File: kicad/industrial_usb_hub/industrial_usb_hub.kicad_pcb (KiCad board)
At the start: 4 copper layers, 55.5 x 64 mm, 86 parts, among them J1 USB3_A, J2 USB_C_Receptacle, J3 USB3_A, J4 USB3_A, J6 USB3_A, U1 USB5744-I_2G, U2 HD3SS3212IRKSR, U3 TUSB321, U4 SY6280, U5 SY6280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

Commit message: routed the USB C cables, fuck that was annoying, but at some point it just, got easier randomly? at an instant, didn't even notice it
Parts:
- moved R24 12.2 mm to (127.1, 114.5)
- moved U3 11.3 mm to (128.5, 117.8)
- moved C24 9.29 mm to (141.9, 112.7)
- moved C23 3.01 mm to (142.0, 110.8)
- moved Y1 2.82 mm to (138.6, 111.2)
- moved C13 2.77 mm to (132.3, 112.2)
- moved U2 2.59 mm to (135.2, 117.1)
- moved C14 2.57 mm to (133.1, 112.2)
- moved R1 2.36 mm to (132.0, 119.8)
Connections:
- net Net-(U1-USB3UP_TXDM) renamed /Hub Controller/USB3UP_TXD_N
- net Net-(U1-USB3UP_TXDP) renamed /Hub Controller/USB3UP_TXD_P
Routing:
- net /Upstream/RX1_N: track 0.00 -> 27.5 mm
- net /Upstream/RX1_P: track 0.00 -> 24.5 mm, vias 0 -> 2
- net /Upstream/TX2_N: track 0.00 -> 16.2 mm
- net Net-(J2-CC2): track 0.00 -> 15.7 mm
- net /Hub Controller/UP_D_N: track 0.00 -> 15.7 mm
- net /Hub Controller/UP_D_P: track 0.00 -> 15.7 mm
- net /Upstream/TX2_P: track 0.00 -> 13.0 mm
- net Net-(J2-CC1): track 0.00 -> 10.5 mm, vias 0 -> 2
- net Net-(U1-XTALO): track 0.00 -> 9.72 mm
- net /Hub Controller/UP_RX_P: track 0.00 -> 8.75 mm, vias 0 -> 1
- net /Hub Controller/UP_RX_N: track 0.00 -> 8.73 mm, vias 0 -> 1
- net Net-(U1-XTALI/CLK_IN): track 0.00 -> 7.84 mm
- net /Upstream/RX2_P: track 0.00 -> 5.03 mm, vias 0 -> 1
- net /Upstream/RX2_N: track 0.00 -> 5.00 mm, vias 0 -> 1
- net /Hub Controller/UP_TX_P: track 0.00 -> 4.12 mm, vias 0 -> 1
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
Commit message: okay okay it seems easier to do differential routing, feels menacing tho
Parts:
- moved C24 6.54 mm to (135.5, 111.6)
- moved C23 6.48 mm to (135.6, 109.8)
- moved C33 0.94 mm to (126.1, 103.2), turned to -90 degrees
- moved C29 0.83 mm to (130.0, 99.5)
- moved C30 0.77 mm to (130.0, 100.2)
- moved R11 0.23 mm to (128.6, 107.0)
- moved R12 0.23 mm to (128.6, 107.8)
- moved R13 0.19 mm to (128.6, 106.3)
- moved R14 0.18 mm to (128.5, 105.6)
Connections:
- C29 pad 1: Net-(U1-USB3DN_TXDP4) -> /Hub Controller/DN_TX_P4
- C29 pad 2: /Downstream/DN_TX_P4 -> /Hub Controller/DN_TX_P4
- C30 pad 1: Net-(U1-USB3DN_TXDM4) -> /Hub Controller/DN_TX_N4
- C30 pad 2: /Downstream/DN_TX_N4 -> /Hub Controller/DN_TX_N4
- J3 pad 8: /Downstream/DN_TX_N4 -> /Hub Controller/DN_TX_N4
- J3 pad 9: /Downstream/DN_TX_P4 -> /Hub Controller/DN_TX_P4
- U1 pad 26: Net-(U1-USB3DN_TXDP4) -> /Hub Controller/DN_TX_P4
- U1 pad 27: Net-(U1-USB3DN_TXDM4) -> /Hub Controller/DN_TX_N4
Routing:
- net /Hub Controller/DN_TX_P4: track 0.00 -> 14.9 mm
- net /Hub Controller/DN_TX_N4: track 0.00 -> 14.0 mm
- net /Downstream/DN_RX_N4: track 0.00 -> 12.1 mm
- net /Downstream/DN_RX_P4: track 0.00 -> 11.4 mm
- net Net-(U2-SEL): track 2.84 -> 13.9 mm, vias 0 -> 1
- net Net-(U3-VBUS_DET): track 0.00 -> 3.82 mm
- net Net-(U1-XTALO): track 9.72 -> 6.03 mm
- net Net-(U1-~{RESET}): track 0.00 -> 3.53 mm
- net Net-(U1-VBUS_DET): track 0.00 -> 3.44 mm
- net Net-(U1-XTALI/CLK_IN): track 7.84 -> 5.85 mm
- net /Hub Controller/SPI_CE_N: track 0.00 -> 1.63 mm
- net /Hub Controller/SPI_DI: track 0.00 -> 1.44 mm
- net /Hub Controller/SPI_CLK: track 0.00 -> 1.39 mm
- net /Hub Controller/SPI_DO: track 0.00 -> 1.29 mm
- net /Downstream/DN_D_P4: track 0.00 -> 0.98 mm, vias 0 -> 1
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
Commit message: done routing, now fixing DRC errors (it's hatin)
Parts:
- C15, C16, C17, C18: moved to B.Cu
- moved C15 8.14 mm to (135.2, 114.0), turned to 180 degrees
- moved C16 7.83 mm to (135.3, 114.8), turned to 180 degrees
- moved C19 4.42 mm to (141.2, 106.3)
- moved C20 4.42 mm to (145.7, 107.6)
- moved R2 4.42 mm to (145.7, 105.8)
- moved U4 4.42 mm to (143.2, 106.3)
- moved C18 3.13 mm to (139.2, 106.0)
- moved C17 3.10 mm to (139.2, 106.7)
- moved C36 1.91 mm to (123.1, 86.7)
- moved R9 1.91 mm to (123.1, 88.2)
- moved U7 1.75 mm to (125.7, 87.2)
- moved R24 1.64 mm to (128.0, 116.0)
- moved C1 1.19 mm to (137.4, 97.5)
- moved C10 1.19 mm to (138.9, 97.5)
- moved C11 1.19 mm to (138.9, 96.8)
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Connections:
- net Net-(U1-USB3DN_TXDM1) renamed /Hub Controller/USB3_DN_TX_N1
- net Net-(U1-USB3DN_TXDM2) renamed /Hub Controller/USB3_DN_TX_N2
- net Net-(U1-USB3DN_TXDM3) renamed /Hub Controller/USB3_DN_TX_N3
- net Net-(U1-USB3DN_TXDP1) renamed /Hub Controller/USB3_DN_TX_P1
- net Net-(U1-USB3DN_TXDP2) renamed /Hub Controller/USB3_DN_TX_P2
- net Net-(U1-USB3DN_TXDP3) renamed /Hub Controller/USB3_DN_TX_P3
- C29 pad 1: /Hub Controller/DN_TX_P4 -> /Hub Controller/USB3_DN_TX_P4
- C29 pad 2: /Hub Controller/DN_TX_P4 -> /Downstream/DN_TX_P4
- C30 pad 1: /Hub Controller/DN_TX_N4 -> /Hub Controller/USB3_DN_TX_N4
- C30 pad 2: /Hub Controller/DN_TX_N4 -> /Downstream/DN_TX_N4
- J3 pad 8: /Hub Controller/DN_TX_N4 -> /Downstream/DN_TX_N4
- J3 pad 9: /Hub Controller/DN_TX_P4 -> /Downstream/DN_TX_P4
- U1 pad 26: /Hub Controller/DN_TX_P4 -> /Hub Controller/USB3_DN_TX_P4
- U1 pad 27: /Hub Controller/DN_TX_N4 -> /Hub Controller/USB3_DN_TX_N4
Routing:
- net GND: track 0.00 -> 71.5 mm, vias 0 -> 20
- net +1V2: track 0.00 -> 44.2 mm, vias 0 -> 7
- net /Downstream/DN_D_P3: track 0.00 -> 41.7 mm, vias 0 -> 1
- net /Downstream/DN_D_N3: track 0.00 -> 41.6 mm, vias 0 -> 1
- net /Downstream/DN_D_N2: track 0.00 -> 38.0 mm, vias 0 -> 1
- net /Downstream/DN_D_P2: track 0.00 -> 38.0 mm, vias 0 -> 1
- net /Downstream/EN2: track 0.00 -> 36.0 mm, vias 0 -> 2
- net /Downstream/DN_RX_N2: track 0.00 -> 35.6 mm, vias 0 -> 1
- net /Downstream/DN_RX_P2: track 0.00 -> 35.6 mm, vias 0 -> 1
- net +3V3: track 0.00 -> 35.0 mm, vias 0 -> 5
- net /Downstream/DN_TX_P3: track 0.00 -> 31.8 mm
- net /Downstream/DN_TX_N3: track 0.00 -> 31.7 mm
- net /Downstream/DN_RX_P3: track 0.00 -> 31.3 mm
- net /Downstream/DN_RX_N3: track 0.00 -> 31.3 mm
- net Net-(J4-VBUS): track 0.00 -> 30.7 mm
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- added copper zone on In2.Cu, net +1V2
- added copper zone on In2.Cu, net +3V3
- added copper zone on In2.Cu, net /Downstream/VBUS
- added copper zone on B.Cu, net GND
- added copper zone on F.Cu, net GND

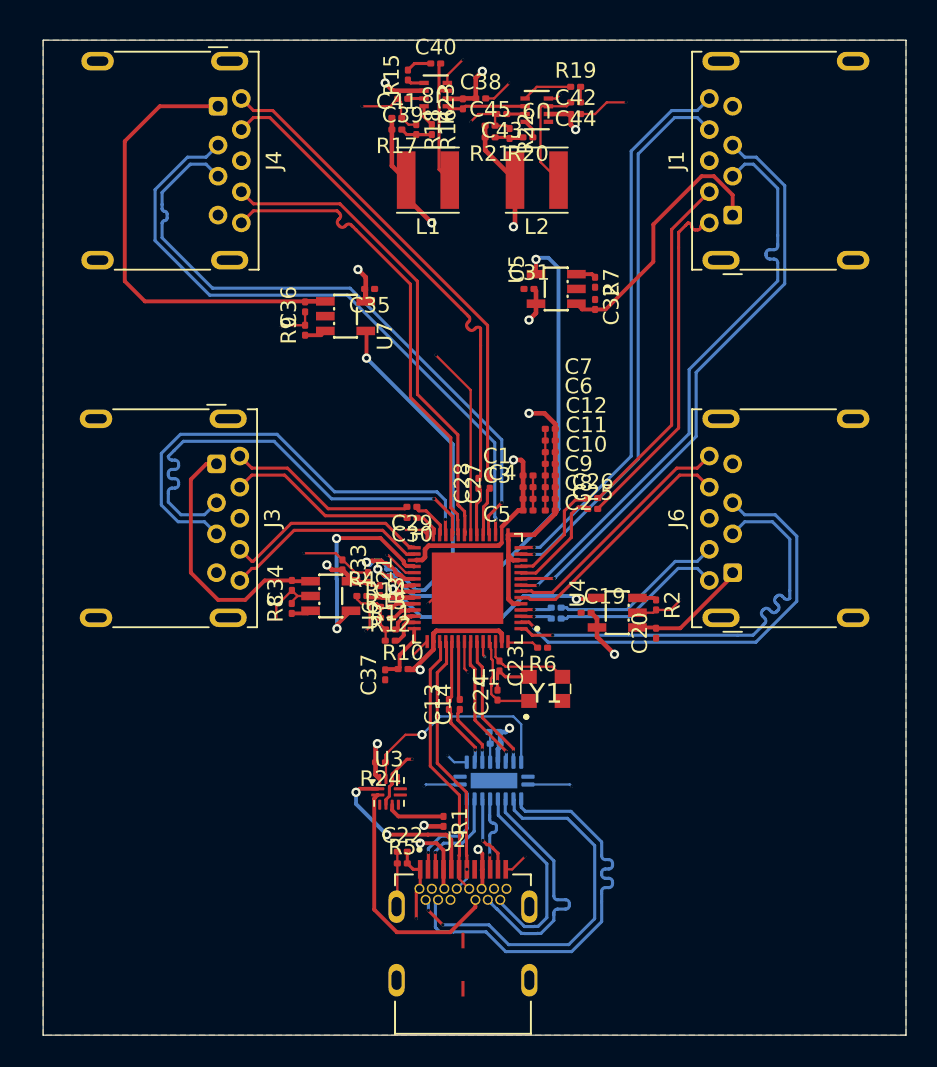
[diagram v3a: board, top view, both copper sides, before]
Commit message: finalized routing, fixed DRC issues, imported the 3D models, all good
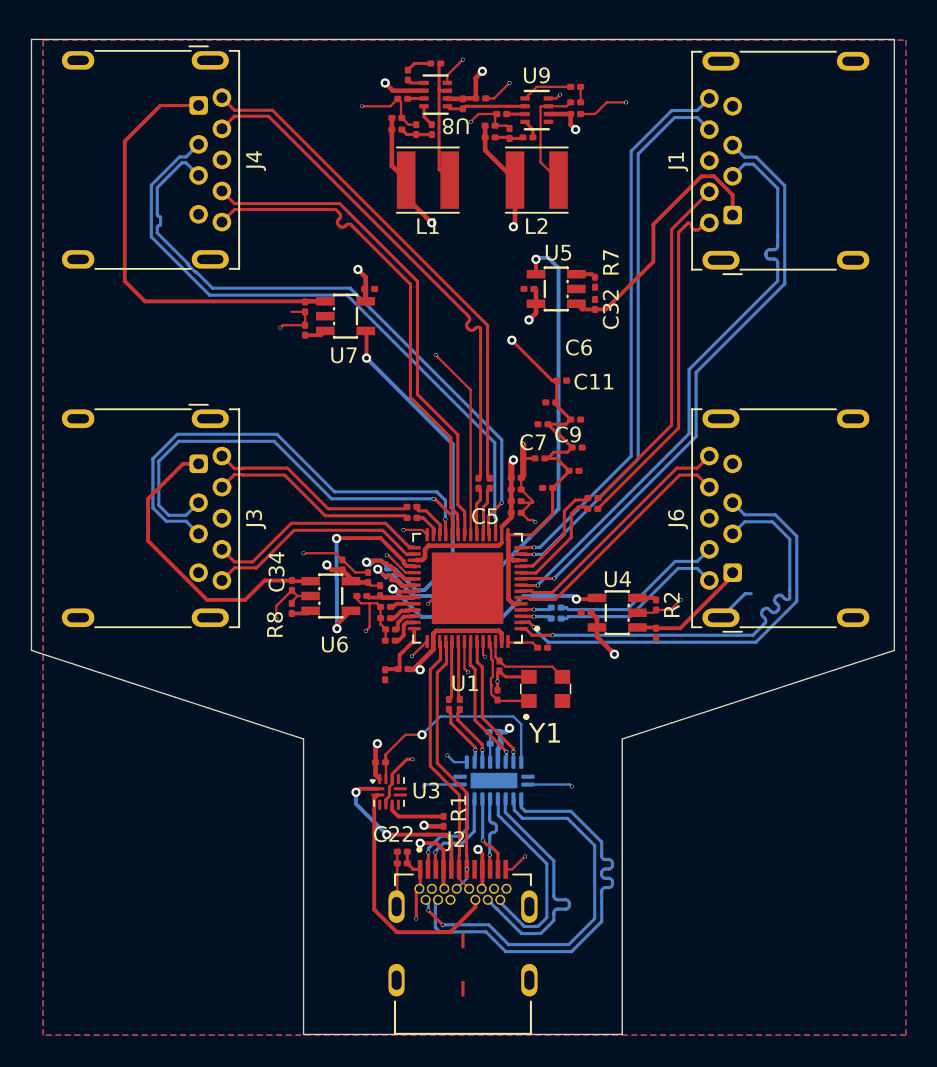
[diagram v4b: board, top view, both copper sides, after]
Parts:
- moved C7 3.18 mm to (139.6, 91.4), turned to 0 degrees
- moved C12 2.66 mm to (140.5, 93.9), turned to 0 degrees
- moved C11 2.59 mm to (138.4, 94.2)
- moved C10 2.50 mm to (140.6, 95.7), turned to 0 degrees
- moved C6 2.45 mm to (138.9, 92.8)
- moved C8 2.36 mm to (140.4, 97.2), turned to 0 degrees
- moved C9 1.97 mm to (138.2, 96.4)
- moved C2 1.46 mm to (138.7, 98.3)
- moved J4 1.25 mm to (116.2, 73.7)
- moved J3 1.15 mm to (116.2, 96.8)
- moved C1 0.77 mm to (136.7, 97.7)
- moved C3 0.77 mm to (136.7, 98.4)
- moved C4 0.77 mm to (136.7, 99.2)
- moved C5 0.77 mm to (136.7, 99.9)
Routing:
- net +1V2: track 44.2 -> 54.1 mm
- net GND: track 71.5 -> 75.1 mm, vias 20 -> 22
- net Net-(J3-VBUS): track 17.0 -> 19.9 mm
- net /Downstream/DN_TX_N4: track 12.2 -> 14.0 mm
- net /Downstream/DN_D_P4: track 30.3 -> 28.6 mm
- net /Downstream/DN_RX_N4: track 13.2 -> 14.9 mm
- net /Downstream/DN_RX_P4: track 13.2 -> 14.9 mm
- net /Downstream/DN_TX_N3: track 31.7 -> 33.0 mm
- net /Downstream/DN_RX_N3: track 31.3 -> 32.6 mm
- net /Downstream/DN_RX_P3: track 31.3 -> 32.6 mm
- net /Downstream/DN_TX_P3: track 31.8 -> 33.0 mm
- net Net-(J4-VBUS): track 30.7 -> 29.5 mm
- net /Downstream/DN_TX_P4: track 12.2 -> 13.4 mm
- net +3V3: track 35.0 -> 34.0 mm
- net /Downstream/DN_D_P3: track 41.7 -> 41.0 mm
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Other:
- outline, holes or cut-outs redrawn

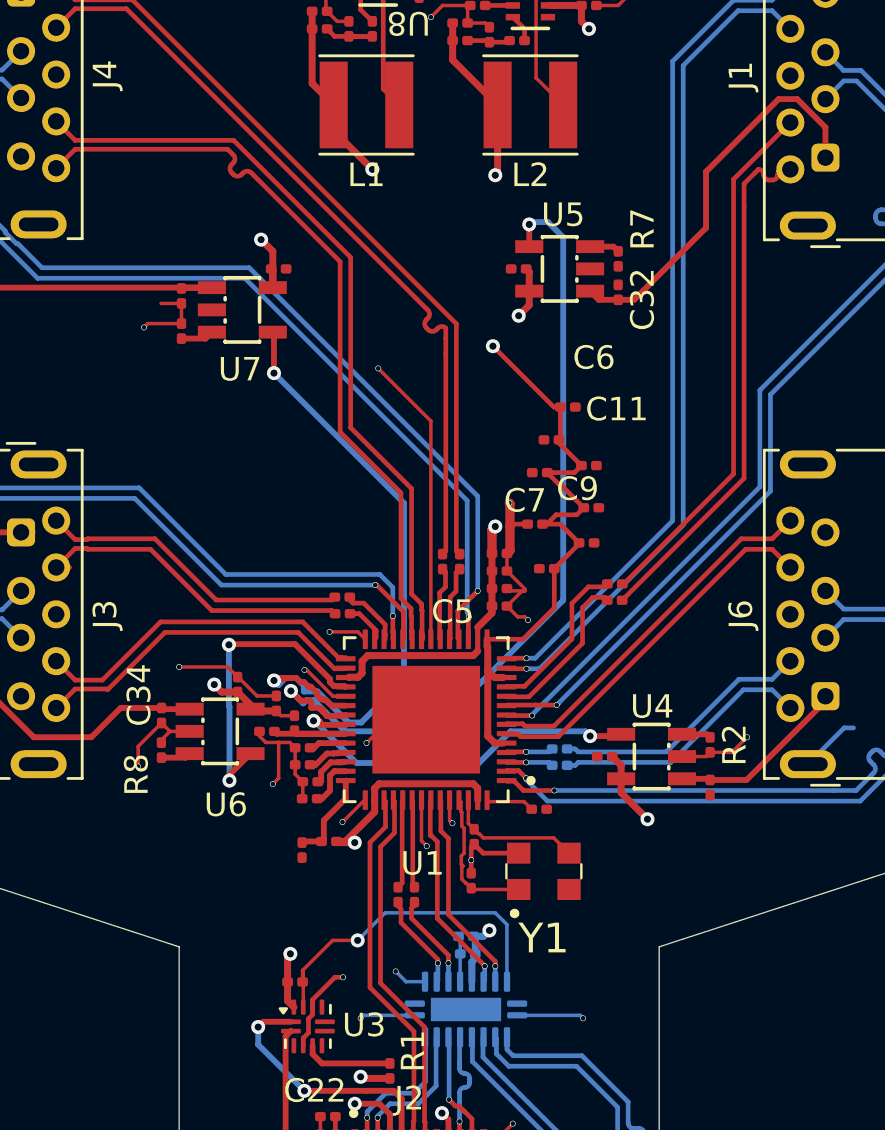
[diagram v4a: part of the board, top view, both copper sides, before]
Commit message: added testpoints
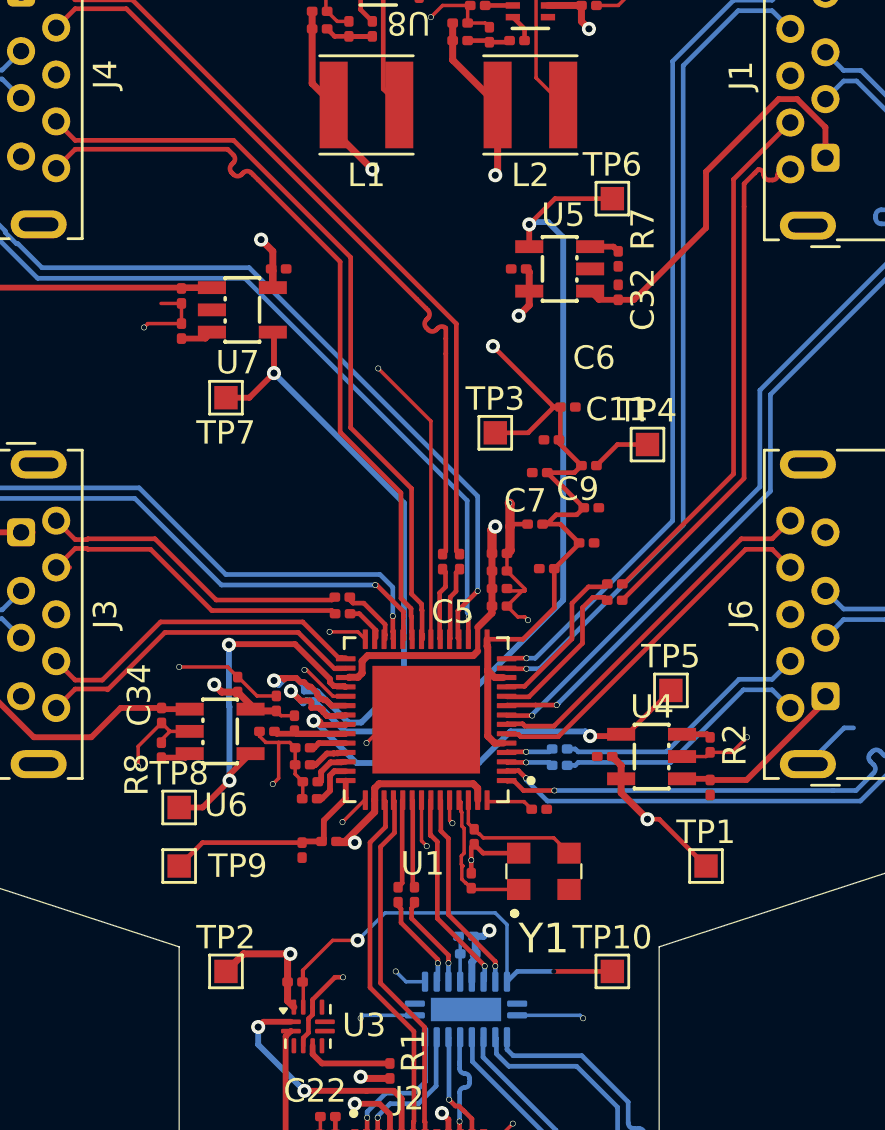
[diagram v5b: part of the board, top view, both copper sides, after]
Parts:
- added TP1: VBUS, TestPoint:TestPoint_Pad_1.0x1.0mm, F.Cu at (145.5, 111.0)
- added TP10: DIR, TestPoint:TestPoint_Pad_1.0x1.0mm, F.Cu at (141.5, 115.5)
- added TP2: 3V3, TestPoint:TestPoint_Pad_1.0x1.0mm, F.Cu at (125.0, 115.5)
- added TP3: 1V2, TestPoint:TestPoint_Pad_1.0x1.0mm, F.Cu at (136.5, 92.5)
- added TP4: GND, TestPoint:TestPoint_Pad_1.0x1.0mm, F.Cu at (143.0, 93.0)
- added TP5: EN1, TestPoint:TestPoint_Pad_1.0x1.0mm, F.Cu at (144.0, 103.5)
- added TP6: EN2, TestPoint:TestPoint_Pad_1.0x1.0mm, F.Cu at (141.5, 82.5)
- added TP7: EN3, TestPoint:TestPoint_Pad_1.0x1.0mm, F.Cu at (125.0, 91.0)
- added TP8: 1V2, TestPoint:TestPoint_Pad_1.0x1.0mm, F.Cu at (123.0, 108.5)
- added TP9: RESET_N, TestPoint:TestPoint_Pad_1.0x1.0mm, F.Cu at (123.0, 111.0)
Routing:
- net Net-(U1-~{RESET}): track 3.88 -> 9.54 mm
- net Net-(U2-SEL): track 14.5 -> 19.2 mm, vias 1 -> 2
- net /Downstream/EN2: track 36.0 -> 40.0 mm
- net /Downstream/VBUS: track 30.0 -> 33.3 mm
- net +3V3: track 34.0 -> 37.1 mm
- net +1V2: track 54.1 -> 57.1 mm
- net /Downstream/EN1: track 16.1 -> 19.0 mm
- net /Downstream/EN4: track 13.2 -> 15.8 mm
- net GND: track 75.1 -> 77.6 mm
- net /Downstream/EN3: track 28.3 -> 30.8 mm
